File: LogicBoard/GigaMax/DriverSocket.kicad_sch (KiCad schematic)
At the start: 3 parts, among them J1 Output, J1 OutputDown, J3 Input

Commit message: moved libs and gigamax version
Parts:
- removed J1: Output, Connector_PinSocket_2.54mm:PinSocket_1x04_P2.54mm_Vertical, symbol Connector_Generic:Conn_01x04
- removed J3: Input, Connector_PinSocket_2.54mm:PinSocket_1x06_P2.54mm_Vertical, symbol Connector_Generic:Conn_01x06
- added C1: 47u 25v Tant, Capacitor_Tantalum_SMD:CP_EIA-7343-31_Kemet-D, symbol Device:C
- added C2, C5: 100n, GigaVescLibs:C_0603_1608Metric_L, symbol Device:C
- added C3, C4: 4.7u 50v, Capacitor_SMD:C_1206_3216Metric, symbol Device:C
- added D1: SS520F, Diode_SMD:D_SMA, symbol Device:D_Schottky
- added D2, D3: DSS34, Diode_SMD:D_SOD-123F, symbol Device:D_Schottky
- added R1: 20k, Resistor_SMD:R_0603_1608Metric, symbol Device:R
- added R2, R3, R4, R5, R6: 2r2, Resistor_SMD:R_0603_1608Metric, symbol Device:R
- added R7, R8: 4.7k, Resistor_SMD:R_0603_1608Metric, symbol Device:R
- added U1: UCC21520DWR, Package_SO:SOIC-16W_7.5x10.3mm_P1.27mm, symbol Driver_FET:UCC21520DW
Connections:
- net +15V: now also C4.1, R2.1, U1.11 (VDDB)
- net +3.3V: now also C1.2, C2.1, U1.3 (VCCI), U1.8 (VCCI)
- net GND: now also J1.1 (Pin_1), C1.1, C2.2, C5.2, R1.2, U1.4 (GND)
- net H: now also U1.1 (INA)
- net L: now also U1.2 (INB)
- net POWER_STAGE_LOCKOUT: now also U1.5 (DIS)
- net PH: now reaches J1.4 (Pin_4)
- net PH: now also D2.2 (A), R4.2, R7.2
- net PL: now reaches J1.3 (Pin_3)
- net PL: now also D3.2 (A), R6.2, R8.2
- net PHASE: now reaches J1.2 (Pin_2)
- net PHASE: now also C3.2, R7.1, U1.14 (VSSA)
- new net: D3.1 (K), R5.2
- new net: C3.1, D1.1 (K), U1.16 (VDDA)
- new net: D1.2 (A), R2.2
- new net: C5.1, R1.1, U1.6 (DT)
- new net: D2.1 (K), R3.2
- new net: R3.1, R4.1, U1.15 (OUTA)
- new net: R5.1, R6.1, U1.10 (OUTB)
- new net PHASE_GROUND: C4.2, R8.1, U1.9 (VSSB)
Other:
- note added: "Or any shottky diode with 200V 5A <850mV forward voltage"
- moved on the sheet: J1

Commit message: cleanup
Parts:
- D2, D3: value DSS34 -> SS34; footprint Diode_SMD:D_SOD-123F -> Diode_SMD:D_SMA; MPN C511866 -> C8678
- R2, R3, R4, R5, R6: value 2r2 -> 2.2
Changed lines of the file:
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@@
       (effects (font (size 1.27 1.27)))
     )
-    (property "Value" "DSS34" (at 186.69 115.57 0)
-      (effects (font (size 1.27 1.27)))
-    )
-    (property "Footprint" "Diode_SMD:D_SOD-123F" (at 186.69 111.76 0)
+    (property "Value" "SS34" (at 186.69 115.57 0)
+      (effects (font (size 1.27 1.27)))
+    )
+    (property "Footprint" "Diode_SMD:D_SMA" (at 186.69 111.76 0)
       (effects (font (size 1.27 1.27)) hide)
     )
@@
       (effects (font (size 1.27 1.27)) hide)
     )
-    (property "MPN" "C511866" (at 186.69 111.76 0)
+    (property "MPN" "C8678" (at 186.69 111.76 0)
       (effects (font (size 1.27 1.27)) hide)
     )
@@
       (effects (font (size 1.27 1.27)))
     )
-    (property "Value" "DSS34" (at 186.3725 78.74 0)
-      (effects (font (size 1.27 1.27)))
-    )
-    (property "Footprint" "Diode_SMD:D_SOD-123F" (at 186.69 82.55 0)
+    (property "Value" "SS34" (at 186.3725 78.74 0)
+      (effects (font (size 1.27 1.27)))
+    )
+    (property "Footprint" "Diode_SMD:D_SMA" (at 186.69 82.55 0)
       (effects (font (size 1.27 1.27)) hide)
     )
@@
       (effects (font (size 1.27 1.27)) hide)
     )
-    (property "MPN" "C511866" (at 186.69 82.55 0)
+    (property "MPN" "C8678" (at 186.69 82.55 0)
       (effects (font (size 1.27 1.27)) hide)
     )
@@
       (effects (font (size 1.27 1.27)))
     )
-    (property "Value" "2r2" (at 173.99 88.9 90)
+    (property "Value" "2.2" (at 173.99 88.9 90)
       (effects (font (size 1.27 1.27)))
     )
@@
       (effects (font (size 1.27 1.27)))
     )
-    (property "Value" "2r2" (at 173.99 111.76 90)
+    (property "Value" "2.2" (at 173.99 111.76 90)
       (effects (font (size 1.27 1.27)))
     )
@@
       (effects (font (size 1.27 1.27)))
     )
-    (property "Value" "2r2" (at 173.99 105.41 90)
+    (property "Value" "2.2" (at 173.99 105.41 90)
       (effects (font (size 1.27 1.27)))
     )
@@
       (effects (font (size 1.27 1.27)))
     )
-    (property "Value" "2r2" (at 173.99 82.55 90)
+    (property "Value" "2.2" (at 173.99 82.55 90)
       (effects (font (size 1.27 1.27)))
     )
@@
       (effects (font (size 1.27 1.27)) (justify left))
     )
-    (property "Value" "2r2" (at 137.16 69.85 0)
+    (property "Value" "2.2" (at 137.16 69.85 0)
       (effects (font (size 1.27 1.27)) (justify left))
     )

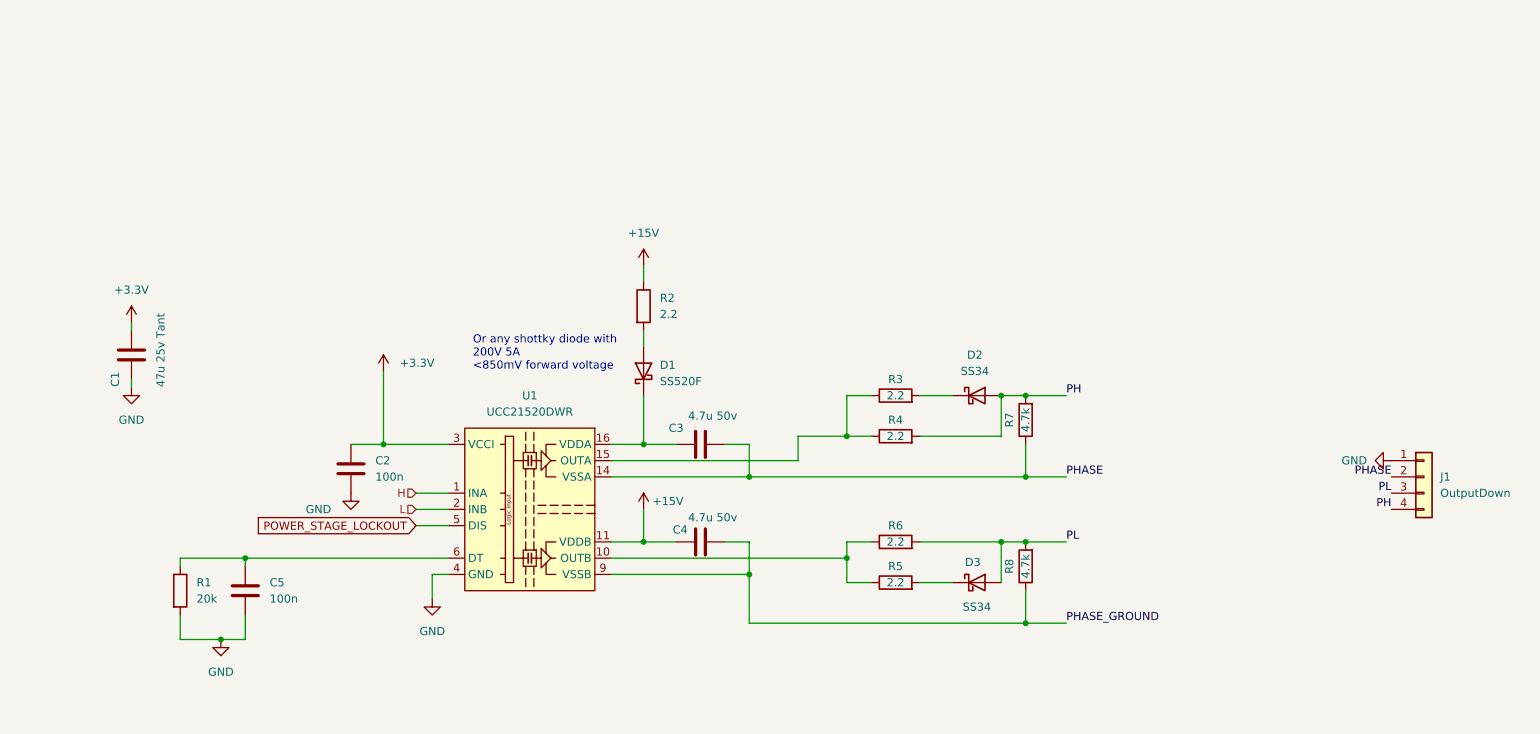
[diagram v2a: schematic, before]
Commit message: v2.8.0 - Small Hall sensors
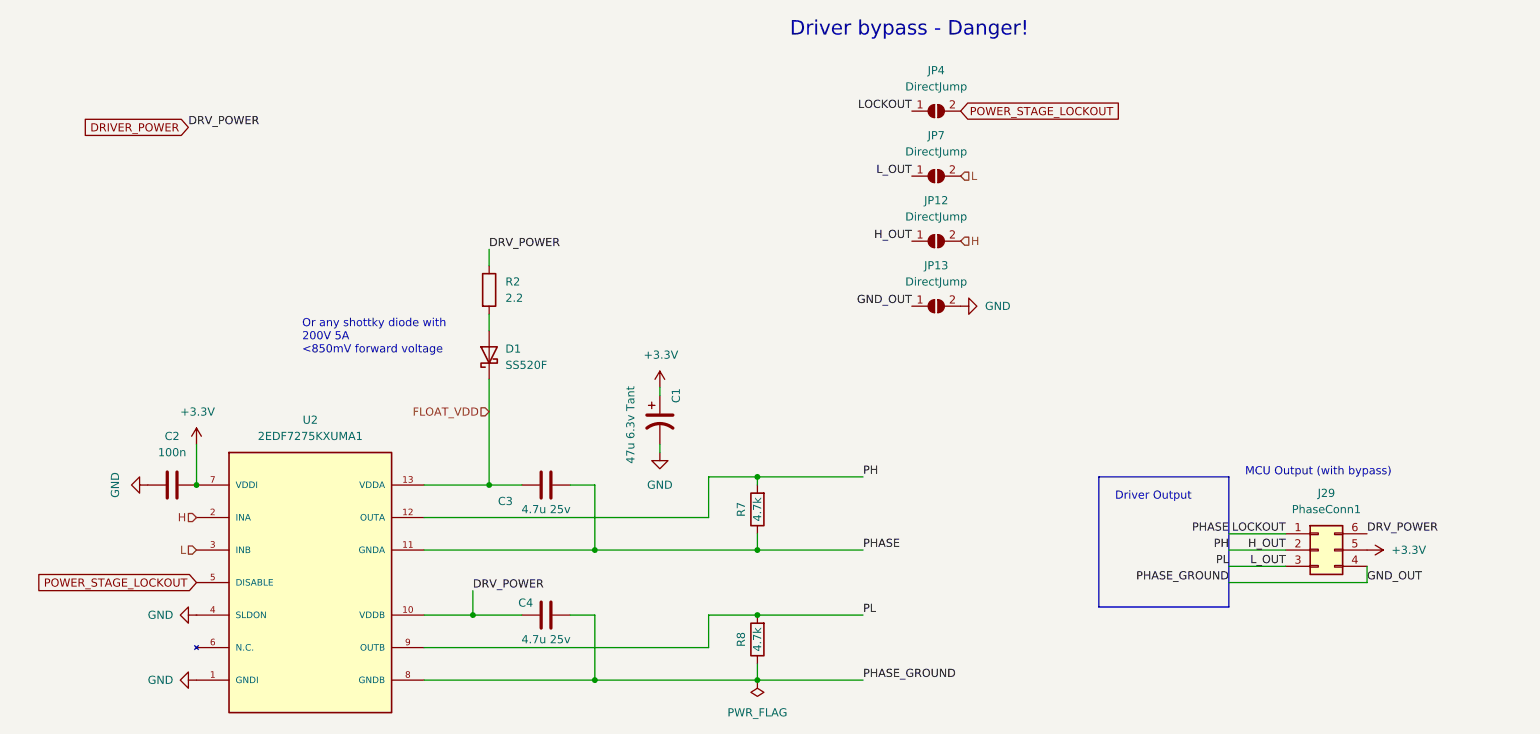
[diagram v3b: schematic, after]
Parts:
- removed C1: 47u 25v Tant, Capacitor_Tantalum_SMD:CP_EIA-7343-31_Kemet-D, symbol Device:C
- removed C5: 100n, GigaVescLibs:C_0603_1608Metric_L, symbol Device:C
- removed D2, D3: SS34, Diode_SMD:D_SMA, symbol Device:D_Schottky
- removed J1: OutputDown, Connector_PinHeader_2.54mm:PinHeader_2x02_P2.54mm_Vertical_SMD, symbol Connector_Generic:Conn_01x04
- removed R1: 20k, Resistor_SMD:R_0603_1608Metric, symbol Device:R
- removed R3, R4, R5, R6: 2.2, Resistor_SMD:R_0603_1608Metric, symbol Device:R
- removed U1: UCC21520DWR, Package_SO:SOIC-16W_7.5x10.3mm_P1.27mm, symbol Driver_FET:UCC21520DW
- added C1: 47u 6.3v Tant, Capacitor_Tantalum_SMD:CP_EIA-3216-18_Kemet-A, symbol Device:C_Polarized_US
- added J29: PhaseConn1, Connector_PinHeader_2.54mm:PinHeader_2x03_P2.54mm_Vertical_SMD, symbol Connector_Generic:Conn_02x03_Counter_Clockwise
- added JP12, JP13, JP4, JP7: DirectJump, GigaVescLibs:SolderJumper0.5mm_Open, symbol Jumper:SolderJumper_2_Open
- added U2: 2EDF7275KXUMA1, GigaVescLibs:IC_2EDF7275KXUMA2, symbol GigaESCSymbols:2EDF7275KXUMA2
- C2: footprint GigaVescLibs:C_0603_1608Metric_L -> Capacitor_SMD:C_0805_2012Metric; MPN C14663 -> C28233
- C3, C4: value 4.7u 50v -> 4.7u 25v; footprint Capacitor_SMD:C_1206_3216Metric -> Capacitor_SMD:C_0805_2012Metric; MPN C29823 -> C1779
- R2: MPN C22939 -> C17521
- R7, R8: MPN C23162 -> C17673
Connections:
- net +3.3V: now also C2.2, C1.1, J29.5 (Pin_5), U2.7 (VDDI); no longer C2.1
- net GND: now also C2.1, C1.2, JP13.2 (B), U2.1 (GNDI), U2.4 (SLDON); no longer C2.2
- net H: now also JP12.2 (B), U2.2 (INA)
- net L: now also JP7.2 (B), U2.3 (INB)
- net POWER_STAGE_LOCKOUT: now also JP4.2 (B), U2.5 (DISABLE)
- net FLOAT_VDD: now reaches C3.1, D1.1 (K)
- net FLOAT_VDD: now also U2.13 (VDDA)
- net +15V renamed DRIVER_POWER
- net DRIVER_POWER: now also J29.6 (Pin_6), U2.10 (VDDB)
- net PH renamed H_OUT
- net H_OUT: now also J29.2 (Pin_2), JP12.1 (A), U2.12 (OUTA)
- net PHASE renamed LOCKOUT
- net LOCKOUT: now also J29.1 (Pin_1), JP4.1 (A), U2.11 (GNDA)
- net PHASE_GROUND renamed GND_OUT
- net GND_OUT: now also J29.4 (Pin_4), JP13.1 (A), U2.8 (GNDB)
- net PL renamed L_OUT
- net L_OUT: now also J29.3 (Pin_3), JP7.1 (A), U2.9 (OUTB)
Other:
- note added: "Driver Output"
- note added: "Driver bypass - Danger!"
- note added: "MCU Output (with bypass)"
